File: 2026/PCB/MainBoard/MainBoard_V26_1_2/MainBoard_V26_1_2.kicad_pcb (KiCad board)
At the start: 2 copper layers, 100 x 65 mm, 85 parts, among them J1 Raspberry_Pi_2_3, J15 TFT3, J16 CAN_CON, J2 fan, J3 MOLEX, J5 Conn_01x05_Socket, J6 Debug, Q1 Q_NMOS_GSD, Q2 Q_NMOS_GSD, SW1 SW_MEC_5E, SW2 Ras_1, SW3 Ras_2, SW4 SW_Wuerth_450301014042, SW5 SW_MEC_5E, SW6 SW_MEC_5E, U1 STM32F446RETx, U10 MPU9250, U2 LMR51460FSQDRRRQ1, U3 MOUDLE-SEEEDUINO-XIAO, U5 MCP1703AT-3302E/CB, U6 BNO055, U8 MAX3051, Y1 CSTNE16M0V530000R0

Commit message: 回路微修正
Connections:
- J1 pad 11: unconnected-(J1-GPIO17-Pad11) -> RAS_AUDIO
- J1 pad 33: RAS_AUDIO -> unconnected-(J1-PWM1/GPIO13-Pad33)
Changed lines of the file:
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@@
 	(net 52 "LED_RAS2")
 	(net 53 "SPI2.CLK")
-	(net 54 "unconnected-(J1-GPIO17-Pad11)")
+	(net 54 "unconnected-(J1-PWM1{slash}GPIO13-Pad33)")
 	(net 55 "R2")
 	(net 56 "unconnected-(J1-3V3-Pad1)_1")
@@
 			(layers "*.Cu" "*.Mask" "F.SilkS")
 			(remove_unused_layers no)
-			(net 54 "unconnected-(J1-GPIO17-Pad11)")
+			(net 48 "RAS_AUDIO")
 			(pinfunction "GPIO17")
-			(pintype "bidirectional+no_connect")
+			(pintype "bidirectional")
 		)
 		(pad "12" thru_hole circle
@@
 			(net 32 "unconnected-(J1-~{CE0}{slash}GPIO8-Pad24)")
 			(pinfunction "~{CE0}/GPIO8")
-			(pintype "bidirectional+no_connect")
+			(pintype "bidirectional")
 		)
 		(pad "25" thru_hole circle
@@
 			(layers "*.Cu" "*.Mask" "F.SilkS")
 			(remove_unused_layers no)
-			(net 48 "RAS_AUDIO")
+			(net 54 "unconnected-(J1-PWM1{slash}GPIO13-Pad33)")
 			(pinfunction "PWM1/GPIO13")
-			(pintype "bidirectional")
+			(pintype "bidirectional+no_connect")
 		)
 		(pad "34" thru_hole circle

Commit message: 電源周り途中
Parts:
- moved R3 2.69 mm to (171.2, 106.7), turned to -90 degrees
- moved R21 1.82 mm to (179.5, 109.9)
- moved R4 1.82 mm to (181.0, 109.9)
- moved R2 1.64 mm to (172.7, 106.7), turned to 90 degrees
- moved C15 1.28 mm to (171.2, 110.9)
- moved R7 0.99 mm to (188.5, 111.5)
- moved C11 0.90 mm to (179.5, 113.5)
- moved C13 0.90 mm to (179.5, 115.0)
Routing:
- net +5V: track 0.00 -> 137.7 mm
- net Net-(C15-Pad2): track 0.00 -> 28.3 mm
- net CANL: track 0.00 -> 26.5 mm
- net CANH: track 0.00 -> 24.4 mm
- net Net-(D9-K): vias 0 -> 1
- net Net-(D8-K): vias 0 -> 1
- net Net-(D7-K): vias 0 -> 1
- net Net-(D3-K): vias 0 -> 1
- net Net-(D15-K): vias 0 -> 1
- net Net-(D14-A): vias 0 -> 1
- net Net-(D13-A): vias 0 -> 1
- net Net-(D11-K): vias 0 -> 1
- net Net-(D10-K): vias 0 -> 1

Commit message: 電源、UI、LED 仮完成
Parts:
- removed D15: LED, LED_SMD:LED_0603_1608Metric_Pad1.05x0.95mm_HandSolder
- removed R17: 1k, Resistor_SMD:R_0603_1608Metric_Pad0.98x0.95mm_HandSolder
- D10, D11, D13, D14, D3, D7, D8, D9: moved to F.Cu
- R12, R13, R14, R15, R16, R18, R19, R6: moved to B.Cu
- moved D10 1.35 mm to (262.4, 98.7), turned to 180 degrees
- moved D11 1.35 mm to (262.4, 104.8), turned to 180 degrees
- moved D13 1.35 mm to (262.4, 100.2), turned to 0 degrees
- moved D14 1.35 mm to (262.4, 101.8), turned to 0 degrees
- moved D3 1.35 mm to (262.4, 103.2), turned to 180 degrees
- moved D7 1.35 mm to (262.4, 94.2), turned to 180 degrees
- moved D8 1.35 mm to (262.4, 95.7), turned to 180 degrees
- moved D9 1.35 mm to (262.4, 97.2), turned to 180 degrees
- moved R12 1.35 mm to (262.4, 94.2), turned to 180 degrees
- moved R13 1.35 mm to (262.4, 95.7), turned to 180 degrees
- moved R14 1.35 mm to (262.4, 97.2), turned to 180 degrees
- moved R15 1.35 mm to (262.4, 98.7), turned to 180 degrees
- moved R16 1.35 mm to (262.4, 104.8), turned to 180 degrees
- moved R18 1.35 mm to (262.4, 100.2), turned to 0 degrees
- moved R19 1.35 mm to (262.4, 101.8), turned to 0 degrees
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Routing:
- net +3.3V: track 0.00 -> 216.2 mm, vias 0 -> 1
- net +5V: track 137.7 -> 255.2 mm, vias 0 -> 1
- net LED0: track 0.00 -> 52.9 mm
- net MISO: track 0.00 -> 50.1 mm
- net SPI1.MOSI: track 0.00 -> 48.3 mm, vias 0 -> 1
- net MOSI: track 0.00 -> 48.3 mm, vias 0 -> 2
- net SCK: track 0.00 -> 45.5 mm
- net HEART_BEAT_LED: track 0.00 -> 39.9 mm, vias 0 -> 2
- net T_CS: track 0.00 -> 39.1 mm, vias 0 -> 1
- net LED2: track 0.00 -> 36.2 mm
- net LCD_LED: track 0.00 -> 35.7 mm
- net LED1: track 0.00 -> 34.6 mm
- net SPI1.CS: track 0.00 -> 32.5 mm
- net R4: track 0.00 -> 32.4 mm
- net SPI1.MISO: track 0.00 -> 30.9 mm
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- added copper zone on B.Cu, net +24V
- added copper zone on B.Cu, net +5V
- added copper zone on B.Cu, net Net-(C15-Pad2)

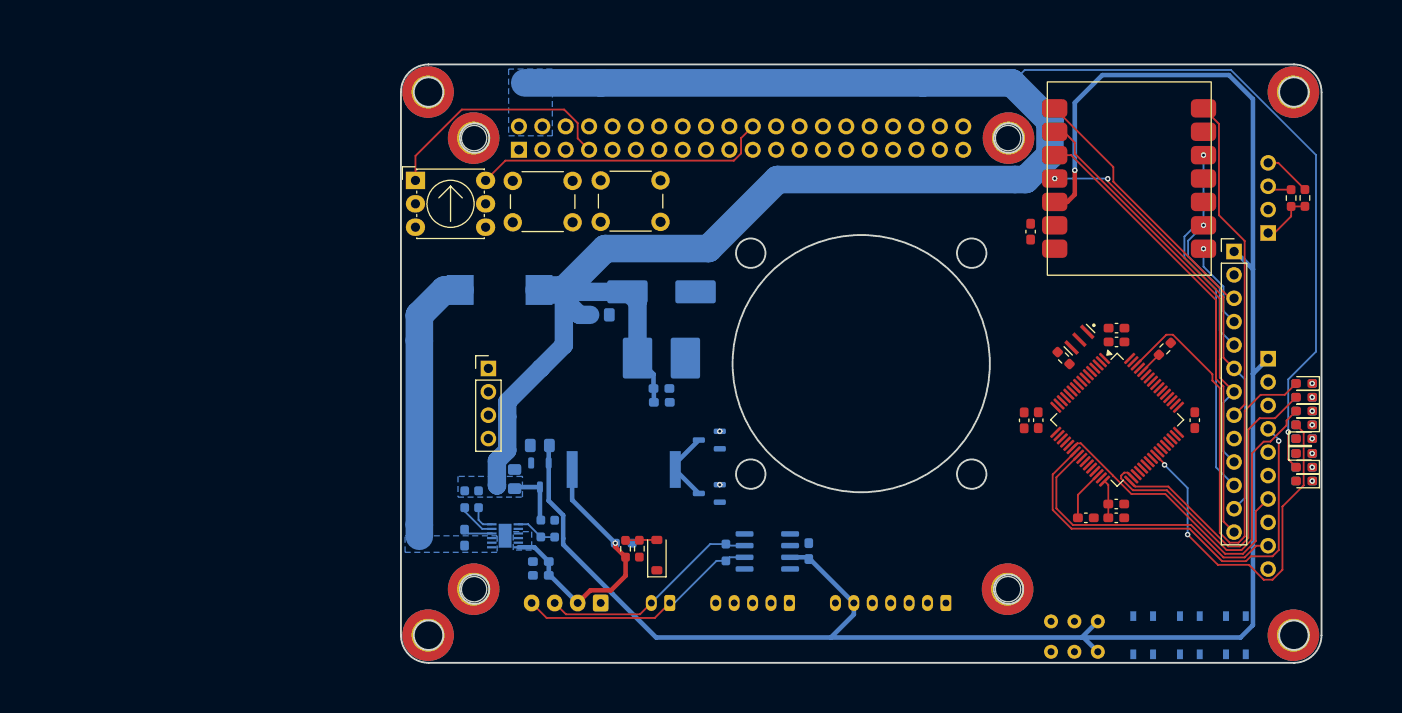
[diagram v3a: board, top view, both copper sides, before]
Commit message: 3.3V配線以外完了
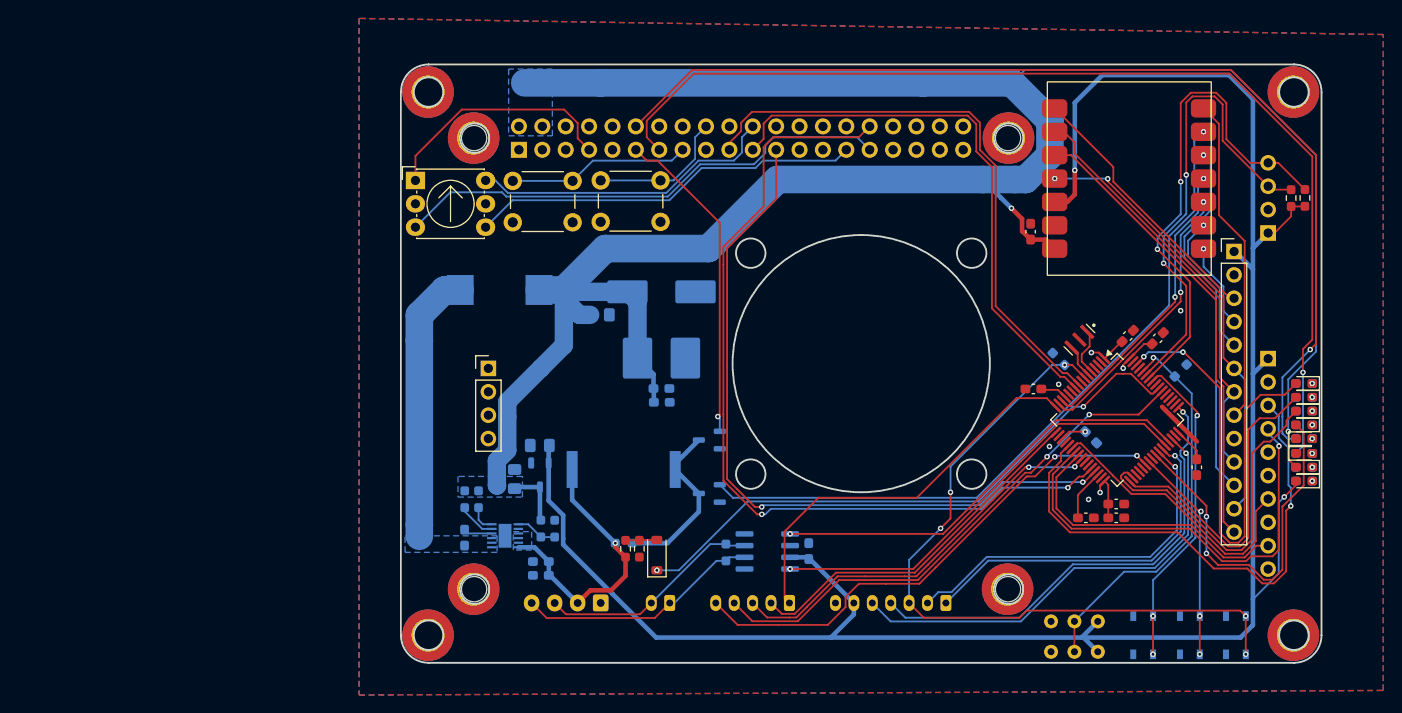
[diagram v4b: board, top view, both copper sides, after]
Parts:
- C3, R1, R5: moved to B.Cu
- moved C3 6.01 mm to (239.2, 100.0), turned to 135 degrees
- moved C5 5.11 mm to (250.8, 103.2), turned to 90 degrees
- moved C6 4.60 mm to (246.5, 89.2), turned to -135 degrees
- moved C7 3.56 mm to (233.0, 94.8), turned to 0 degrees
- moved R1 2.92 mm to (249.0, 92.8)
- moved C2 1.38 mm to (243.2, 89.0), turned to -135 degrees
- moved R5 0.54 mm to (235.8, 91.5)
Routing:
- net LED_RAS2: track 0.00 -> 114.9 mm, vias 0 -> 1
- net LED_RAS1: track 0.00 -> 113.7 mm, vias 0 -> 1
- net SPI2.CS: track 0.00 -> 94.1 mm, vias 0 -> 2
- net SPI2.CLK: track 0.00 -> 80.8 mm, vias 0 -> 2
- net UI_Audio: track 0.00 -> 78.5 mm
- net NRST: track 0.00 -> 78.4 mm, vias 0 -> 5
- net BATTERY_MEASURE: track 0.00 -> 64.5 mm, vias 0 -> 2
- net SPI2.MOSI: track 0.00 -> 63.6 mm
- net SPI2.MISO: track 0.00 -> 60.5 mm
- net MD3_TX: track 0.00 -> 57.7 mm, vias 0 -> 2
- net SPI1.CLK: track 0.00 -> 56.9 mm, vias 0 -> 1
- net MD4_TX: track 0.00 -> 56.4 mm, vias 0 -> 2
- net R3: track 0.00 -> 54.8 mm
- net SWCLK: track 0.00 -> 51.0 mm, vias 0 -> 1
- net SWDIO: track 0.00 -> 50.2 mm, vias 0 -> 1
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- added copper zone on B.Cu, net GND
- added copper zone on F.Cu, net GND

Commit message: ADCピン修正、V2仮完成
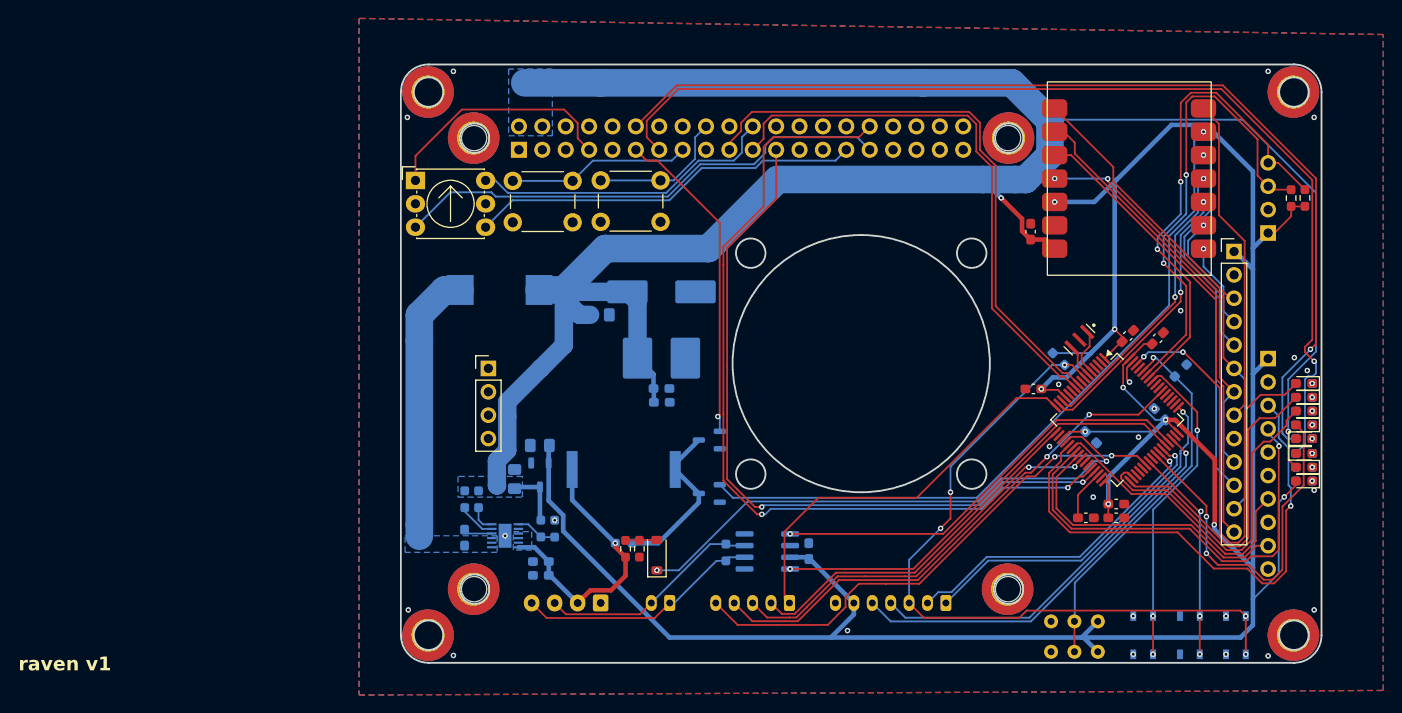
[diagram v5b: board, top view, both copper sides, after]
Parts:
- C5: moved to B.Cu
- moved C5 7.00 mm to (246.8, 97.5), turned to -45 degrees
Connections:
- U1 pad 20: unconnected-(U1-PA4-Pad20) -> BATTERY_MEASURE
- U1 pad 55: BATTERY_MEASURE -> unconnected-(U1-PB3-Pad55)
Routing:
- net +3.3V: track 258.5 -> 313.2 mm, vias 6 -> 9
- net +5V: track 266.9 -> 257.7 mm
- net BATTERY_MEASURE: track 64.5 -> 59.5 mm
- net UART1_TX: track 39.8 -> 34.8 mm
- net UART1_RX: track 38.9 -> 34.1 mm
- net SWCLK: track 51.0 -> 46.2 mm
- net SWDIO: track 50.2 -> 45.5 mm
- net LED_RAS1: track 113.7 -> 110.8 mm
- net GND: track 0.00 -> 2.61 mm, vias 4 -> 23
- net Net-(SW4-B): track 43.2 -> 41.1 mm
- net LED_RAS2: track 114.9 -> 113.3 mm
- net I2C_SCL: track 54.8 -> 53.7 mm
- net Net-(Q1-D): track 18.6 -> 18.0 mm
- net (no net): vias 0 -> 2
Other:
- board text added: "MainBoard V26.1.2"
- board text added: "raven v1"
- board text removed: "MainBoard V26.1.1"

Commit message: モニター位置修正中
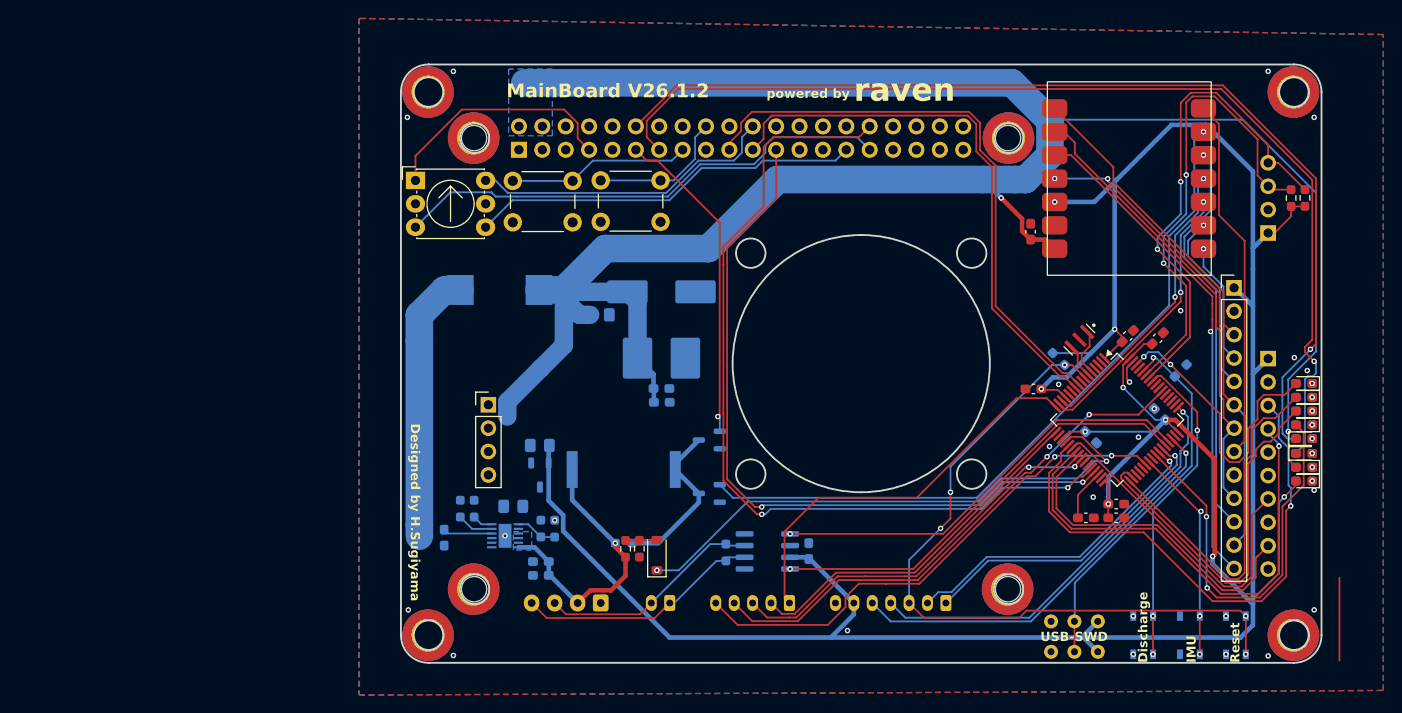
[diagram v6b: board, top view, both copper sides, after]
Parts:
- moved J15 3.95 mm to (173.8, 96.5)
- moved U4 3.95 mm to (254.8, 83.8)
- moved C18 2.97 mm to (176.5, 107.5), turned to 180 degrees
- moved C15 2.21 mm to (169.0, 110.9)
- moved R2 1.13 mm to (172.2, 107.8)
- moved R3 1.13 mm to (170.8, 107.8)
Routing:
- net LED0: track 50.9 -> 31.6 mm
- net +5V: track 257.7 -> 243.4 mm
- net LED2: track 36.2 -> 41.2 mm
- net SPI1.MISO: track 30.9 -> 35.8 mm
- net LED1: track 34.6 -> 39.3 mm
- net SPI1.MOSI: track 48.4 -> 52.8 mm
- net SPI1.CS: track 32.5 -> 36.7 mm
- net MISO: track 50.1 -> 54.2 mm, vias 0 -> 1
- net +3.3V: track 313.2 -> 317.3 mm
- net HEART_BEAT_LED: track 39.9 -> 44.0 mm
- net D/C: track 15.8 -> 19.7 mm
- net T_CS: track 39.7 -> 43.7 mm
- net Reset: track 9.30 -> 13.2 mm
- net LCD_LED: track 35.7 -> 39.6 mm
- net SCK: track 45.5 -> 49.4 mm
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- removed copper zone on B.Cu, net Net-(C15-Pad2)
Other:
- board text added: "Designed by H.Sugiyama"
- board text added: "Discharge"
- board text added: "IMU"
- board text added: "Reset"
- board text added: "USB-SWD"
- board text added: "powered by"
- board text added: "raven"
- board text removed: "Designed by Haruki Sugiyama"
- board text removed: "raven v1"

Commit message: モニター位置修正完了
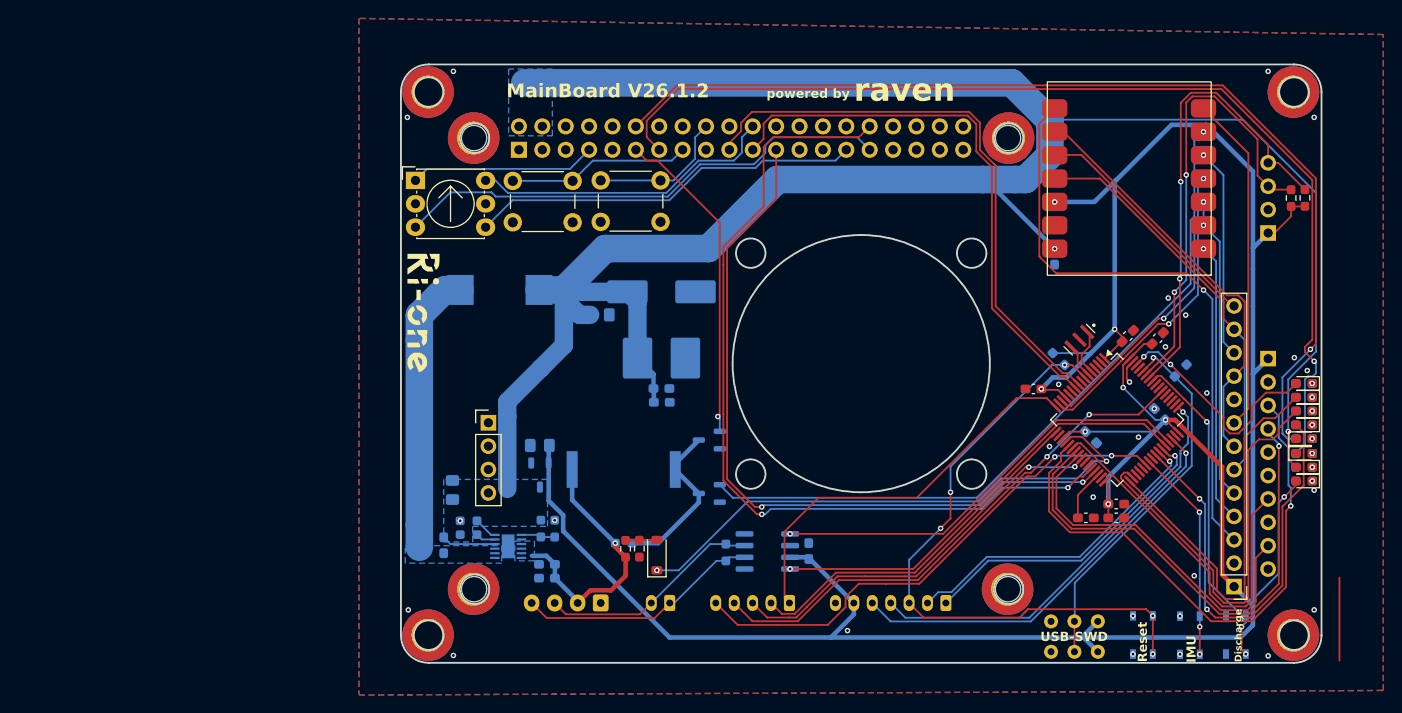
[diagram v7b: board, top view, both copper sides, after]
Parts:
- added G***: LOGO, 0_Library:rione, F.Cu at (166.8, 86.5)
- C12: moved to B.Cu
- moved U4 32.4 mm to (254.8, 116.2), turned to 180 degrees
- moved SW1 10.1 mm to (244.9, 121.5)
- moved SW6 10.1 mm to (255.0, 121.5)
- moved C18 6.83 mm to (169.9, 105.7), turned to 90 degrees
- moved C12 3.76 mm to (235.3, 80.4), turned to -90 degrees
- moved R3 2.96 mm to (171.7, 110.6), turned to 0 degrees
- moved J15 1.95 mm to (173.8, 98.4)
- moved R2 1.45 mm to (171.7, 109.1), turned to 180 degrees
- moved U2 1.20 mm to (175.9, 111.8)
- moved C15 0.83 mm to (168.9, 111.7)
- moved C11 0.73 mm to (180.2, 113.8)
- moved C13 0.73 mm to (180.2, 115.3)
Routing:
- net LED_CS: track 32.6 -> 64.6 mm, vias 0 -> 1
- net MISO: track 54.2 -> 26.3 mm, vias 1 -> 0
- net T_CS: track 43.7 -> 22.8 mm
- net Reset: track 13.2 -> 30.5 mm
- net D/C: track 19.7 -> 30.5 mm
- net NRST: track 78.4 -> 69.0 mm
- net MOSI: track 52.2 -> 43.5 mm, vias 2 -> 0
- net +5V: track 243.4 -> 250.4 mm
- net LED0: track 31.6 -> 25.4 mm
- net R1: track 26.4 -> 20.2 mm
- net LED2: track 41.2 -> 46.3 mm
- net LED1: track 39.3 -> 44.1 mm
- net SPI1.MISO: track 35.8 -> 40.5 mm
- net HEART_BEAT_LED: track 44.0 -> 47.9 mm
- net SPI1.CS: track 36.7 -> 40.0 mm
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- added copper zone on B.Cu, net Net-(C15-Pad2)

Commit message: 配線完了
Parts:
- added G***: LOGO, 0_Library:RAVEN_LOGO_v0_1_1, F.Cu at (168.5, 82.6)
- moved G*** 58.8 mm to (220.1, 61.8), turned to 0 degrees
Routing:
- net SPI1.MOSI: track 55.2 -> 54.7 mm
- net SPI1.CLK: track 61.3 -> 60.7 mm
- net SPI1.CS: track 40.0 -> 39.5 mm
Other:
- board text added: "LED0 LED1 LED2 HB"
- board text added: "Ras1 Ras2 5V 3V3"
